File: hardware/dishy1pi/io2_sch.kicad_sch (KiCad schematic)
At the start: 32 parts, among them J6 TerminalBlock_9x2.54mm, J7 TerminalBlock_6x2.54mm, Q3 LTV-847S, Q4 LTV-847S, U10 LTV-847S, U11 LTV-827S-TA1, U12 LTV-817S-TA1

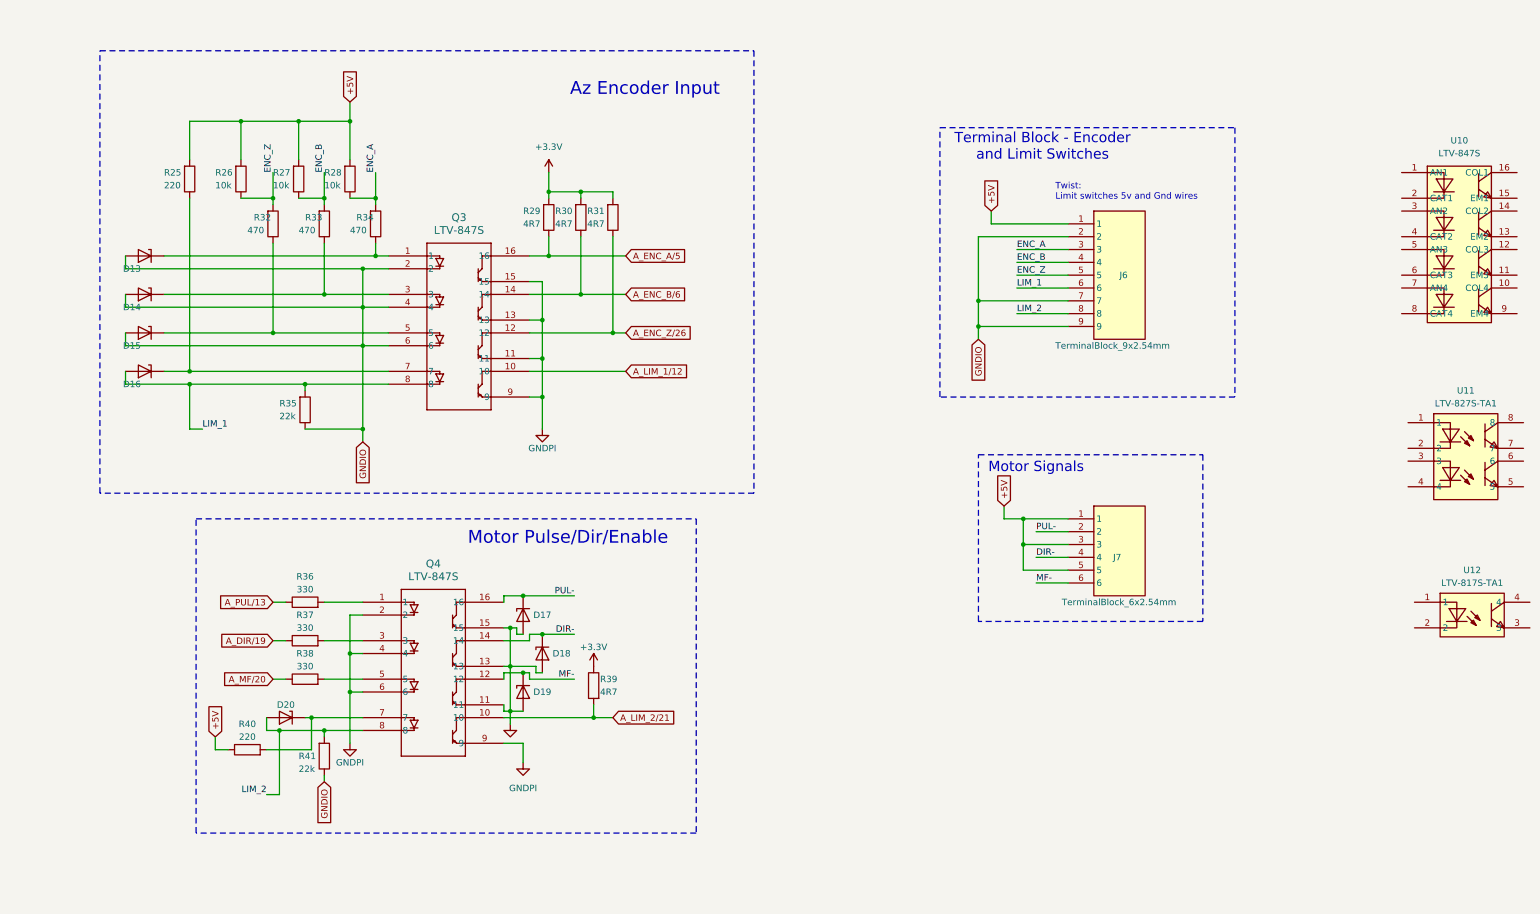
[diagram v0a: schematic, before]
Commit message: Parts place in PCB layout
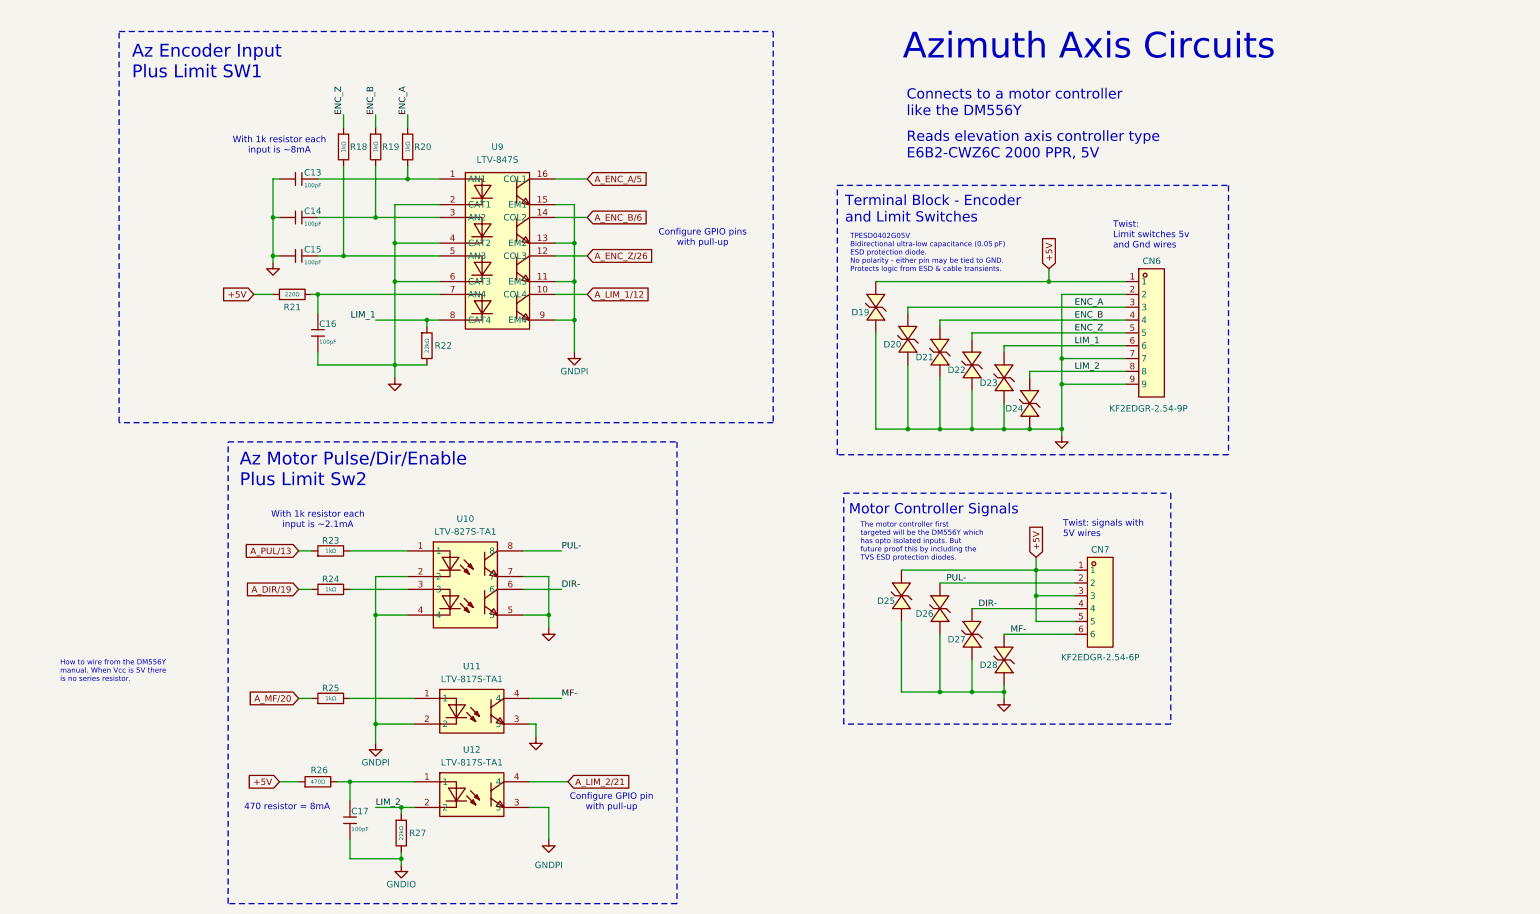
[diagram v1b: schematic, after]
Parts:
- removed D13, D14, D15, D16, D17, D18, D19, D20: TPESD0402G05V, Diode_SMD:D_0402_1005Metric, symbol Diode:PESD5V0L1UL
- removed J6: TerminalBlock_9x2.54mm, DishFootprints:TerminalBlock_9x2.54mm, symbol DishSympols:TerminalBlock_9x2.54mm
- removed J7: TerminalBlock_6x2.54mm, DishFootprints:TerminalBlock_6x2.54mm, symbol DishSympols:TerminalBlock_6x2.54mm
- removed Q3, Q4: LTV-847S, DishFootprints:ACPL-847-300E, symbol DishSympols:ACPL-847-300E
- removed R25, R40: 220, Resistor_SMD:R_0402_1005Metric, symbol Device:R
- removed R26, R27, R28: 10k, Resistor_SMD:R_0402_1005Metric, symbol Device:R
- removed R29, R30, R31, R39: 4R7, Resistor_SMD:R_0402_1005Metric, symbol Device:R
- removed R32, R33, R34: 470, Resistor_SMD:R_0402_1005Metric, symbol Device:R
- removed R35: 22k, Resistor_SMD:R_0201_0603Metric, symbol Device:R
- removed R36, R37, R38: 330, Resistor_SMD:R_0402_1005Metric, symbol Device:R
- removed R41: 22k, Resistor_SMD:R_0402_1005Metric, symbol Device:R
- removed U10: LTV-847S, MyParts:SMD-16_L20.0-W6.5-P2.54-LS10.2-BL, symbol MyParts:LTV-847S
- removed U11: LTV-827S-TA1, MyParts:SMD-8_L9.8-W6.6-P2.54-LS10.3-BL, symbol MyParts:LTV-827S-TA1
- added C13, C14, C15, C16, C17: 100pF, PCM_JLCPCB:C_0402, symbol PCM_JLCPCB-Capacitors:0402,100pF
- added CN6: KF2EDGR-2.54-9P, MyParts:CONN-TH_9P-P2.54_KF2EDGR-2.54-9P, symbol MyParts:KF2EDGR-2.54-9P
- added CN7: KF2EDGR-2.54-6P, MyParts:CONN-TH_KF2EDGR-2.54-6P, symbol MyParts:KF2EDGR-2.54-6P
- added D19, D20, D21, D22, D23, D24, D25, D26, D27, D28: TPESD0402G05V, MyParts:D0402-BI, symbol MyParts:TPESD0402G05V
- added R18, R19, R20, R23, R24, R25: 1kΩ, PCM_JLCPCB:R_0402, symbol PCM_JLCPCB-Resistors:0402,1kΩ
- added R21: 220Ω, PCM_JLCPCB:R_0402, symbol PCM_JLCPCB-Resistors:0402,220Ω
- added R22, R27: 22kΩ, PCM_JLCPCB:R_0402, symbol PCM_JLCPCB-Resistors:0402,22kΩ
- added R26: 470Ω, PCM_JLCPCB:R_0402, symbol PCM_JLCPCB-Resistors:0402,470Ω
- added U10: LTV-827S-TA1, MyParts:LTV827S-TA1, symbol MyParts:LTV-827S-TA1
- added U11: LTV-817S-TA1, MyParts:LTV817S, symbol MyParts:LTV-817S-TA1
- added U9: LTV-847S, myparts:SMD-16_L20.0-W6.5-P2.54-LS10.2-BL, symbol MyParts:LTV-847S
- U12: footprint MyParts:OPTO-SMD-4_L4.6-W6.5-P2.54-LS10.3-BL -> MyParts:LTV817S
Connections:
- net +5V: now also CN6.1, CN7.1, CN7.3, CN7.5, D19.1 (K), D25.1 (K), R21.1, R26.1
- net A_DIR/19: now also R24.1
- net A_ENC_A/5: now also U9.16 (COL1)
- net A_ENC_B/6: now also U9.14 (COL2)
- net A_ENC_Z/26: now also U9.12 (COL3)
- net A_LIM_1/12: now also U9.10 (COL4)
- net A_LIM_2/21: now also U12.4
- net A_MF/20: now also R25.1
- net A_PUL/13: now also R23.1
- net DIR-: now also CN7.4, D27.1 (K), U10.6
- net ENC_A: now also CN6.3, D20.1 (K), R20.1
- net ENC_B: now also CN6.4, D21.1 (K), R19.1
- net ENC_Z: now also CN6.5, D22.1 (K), R18.1
- net GNDIO: now also C13.1, C14.1, C15.1, C16.2, C17.2, CN6.2, CN6.7, CN6.9, D19.2 (A), D20.2 (A), D21.2 (A), D22.2 (A), D23.2 (A), D24.2 (A), D25.2 (A), D26.2 (A), D27.2 (A), D28.2 (A), R22.2, R27.2, U10.5, U10.7, U11.3, U9.2 (CAT1), U9.4 (CAT2), U9.6 (CAT3)
- net GNDPI: now also U12.3, U10.2, U10.4, U11.2, U9.11 (EM3), U9.13 (EM2), U9.15 (EM1), U9.9 (EM4)
- net LIM_1: now also CN6.6, D23.1 (K), R22.1, U9.8 (CAT4)
- net LIM_2: now also U12.2, CN6.8, D24.1 (K), R27.1
- net MF-: now also CN7.6, D28.1 (K), U11.4
- net PUL-: now also CN7.2, D26.1 (K), U10.8
- net at U12.1: now also C17.1, R26.2
- new net: C13.2, R20.2, U9.1 (AN1)
- new net: R23.2, U10.1
- new net: R24.2, U10.3
- new net: C16.1, R21.2, U9.7 (AN4)
- new net: R25.2, U11.1
- new net: C14.2, R19.2, U9.3 (AN2)
- new net: C15.2, R18.2, U9.5 (AN3)
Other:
- note added: "470 resistor = 8mA"
- note added: "Az Encoder Input Plus Limit SW1"
- note added: "Az Motor Pulse/Dir/Enable Plus Limit Sw2"
- note added: "Azimuth Axis Circuits"
- note added: "Configure GPIO pin with pull-up"
- note added: "Configure GPIO pins with pull-up"
- note added: "Connects to a motor controller like the DM556Y"
- note added: "How to wire from the DM556Y manual. When Vcc is 5V there is no series resistor."
- note added: "Motor Controller Signals"
- note added: "Reads elevation axis controller type E6B2-CWZ6C 2000 PPR, 5V"
- note added: "TPESD0402G05V Bidirectional ultra-low capacitance (0.05 pF) ESD protection diode. No polarity - either pin may be tied to GND. Protects logic from ESD & cable transients."
- note added: "The motor controller first targeted will be the DM556Y which has opto isolated inputs. But future proof this by including the TVS ESD protection diodes."
- note added: "Twist: signals with 5V wires"
- note added: "With 1k resistor each input is ~2.1mA"
- note added: "With 1k resistor each input is ~8mA"
- note removed: "Az Encoder Input"
- note removed: "Motor Pulse/Dir/Enable"
- note removed: "Motor Signals"
- company: (none) -> JRDish

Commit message: Ground and Power planes placed
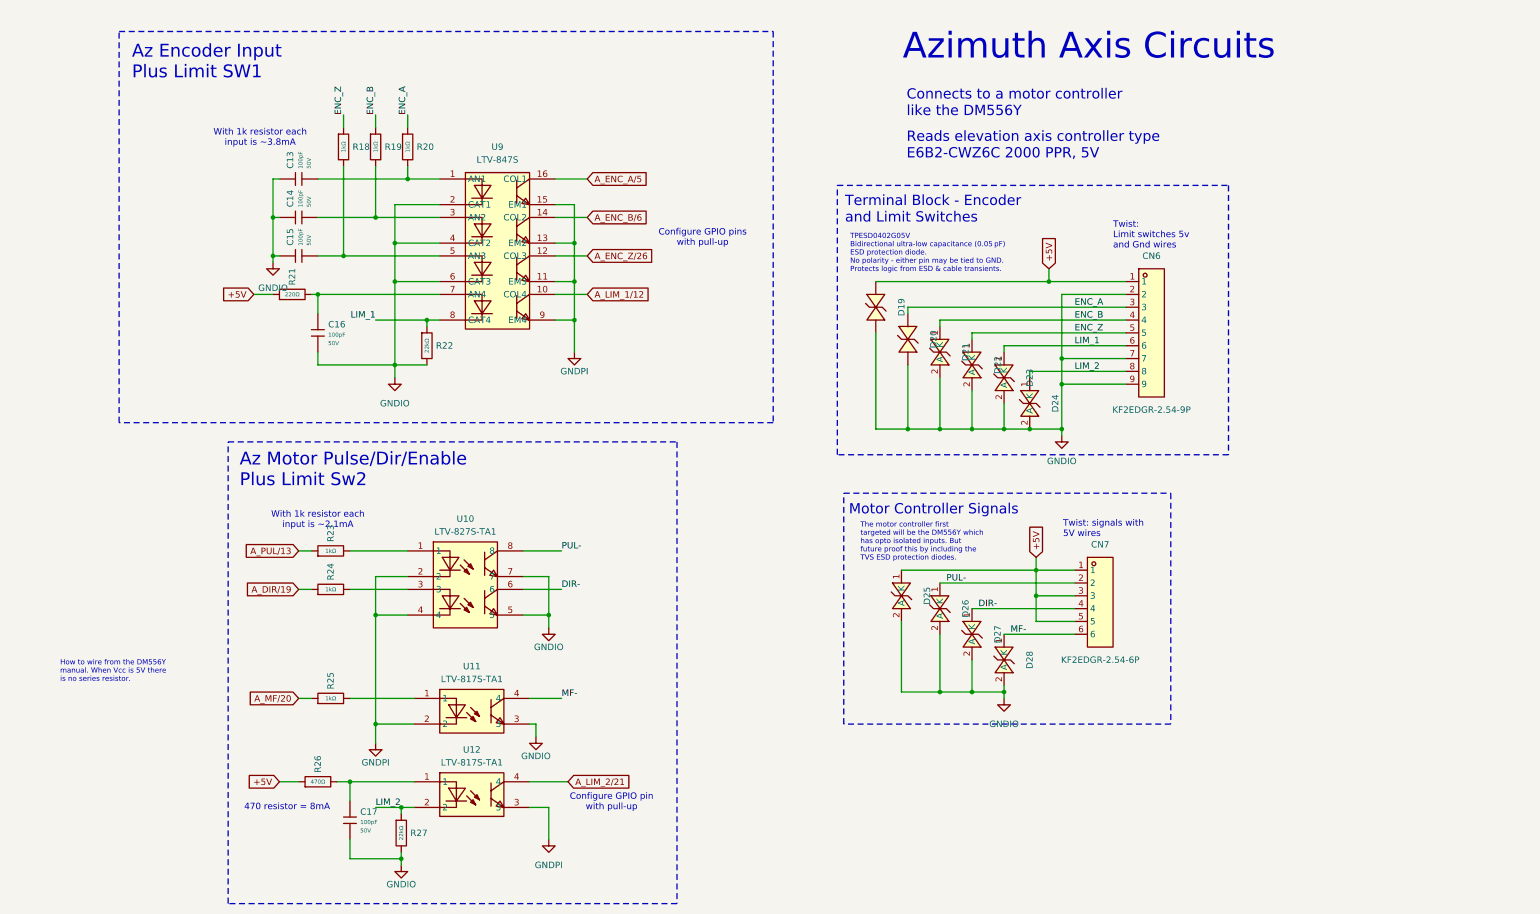
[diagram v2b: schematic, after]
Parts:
- U9: footprint myparts:SMD-16_L20.0-W6.5-P2.54-LS10.2-BL -> MyParts:SMD-16_L20.0-W6.5-P2.54-LS10.2-BL
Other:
- note added: "With 1k resistor each input is ~3.8mA"
- note removed: "With 1k resistor each input is ~8mA"
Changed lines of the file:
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@@
 		)
 	)
-	(text "With 1k resistor each \ninput is ~8mA"
+	(text "With 1k resistor each \ninput is ~3.8mA"
 		(exclude_from_sim no)
-		(at 68.58 44.196 0)
+		(at 64.77 42.672 0)
 		(effects
 			(font
@@
 		(dnp no)
 		(property "Reference" "D21"
-			(at 196.342 86.106 90)
+			(at 204.47 85.09 0)
 			(effects
 				(font
@@
 		(dnp no)
 		(property "Reference" "D27"
-			(at 202.692 141.986 90)
+			(at 210.82 140.97 0)
 			(effects
 				(font
@@
 		(dnp no)
 		(property "Reference" "R26"
-			(at 76.454 167.894 90)
+			(at 76.2 168.402 0)
 			(effects
 				(font
 					(size 1.27 1.27)
 				)
+				(justify left)
 			)
 		)
@@
 		(dnp no)
 		(property "Reference" "D25"
-			(at 188.722 134.366 90)
+			(at 196.85 133.35 0)
 			(effects
 				(font
@@
 	)
 	(symbol
+		(lib_name "TPESD0402G05V_2")
 		(lib_id "MyParts:TPESD0402G05V")
 		(at 186.69 76.2 270)
@@
 		(dnp no)
 		(property "Reference" "D19"
-			(at 183.642 77.216 90)
+			(at 191.77 76.2 0)
 			(effects
 				(font
@@
 		(dnp no)
 		(property "Reference" "D22"
-			(at 202.692 88.646 90)
+			(at 210.82 87.63 0)
 			(effects
 				(font
@@
 					(size 1.27 1.27)
 				)
-				(hide yes)
 			)
 		)
@@
 		(dnp no)
 		(fields_autoplaced yes)
-		(property "Reference" "#PWR039"
+		(property "Reference" "#PWR39"
 			(at 212.09 160.02 0)
 			(effects
@@
 		)
 		(property "Value" "GNDIO"
-			(at 212.0899 157.48 90)
+			(at 212.09 158.75 0)
 			(effects
 				(font
 					(size 1.27 1.27)
 				)
-				(justify right)
-				(hide yes)
 			)
 		)
@@
 			(project "DishyPi1"
 				(path "/e63e39d7-6ac0-4ffd-8aa3-1841a4541b55/ce2ab250-a57c-49c3-a7e8-2e9dc039f394"
-					(reference "#PWR039")
+					(reference "#PWR39")
 					(unit 1)
 				)
@@
 		(dnp no)
 		(property "Reference" "R20"
-			(at 95.25 44.45 0)
+			(at 95.758 44.45 0)
 			(effects
 				(font
@@
 					(size 1.27 1.27)
 				)
-				(hide yes)
 			)
 		)
@@
 		(dnp no)
 		(property "Reference" "R22"
-			(at 99.314 83.82 0)
+			(at 99.568 83.82 0)
 			(effects
 				(font
@@
 	)
 	(symbol
+		(lib_name "TPESD0402G05V_1")
 		(lib_id "MyParts:TPESD0402G05V")
 		(at 193.04 82.55 270)
@@
 		(dnp no)
 		(property "Reference" "D20"
-			(at 189.992 83.566 90)
+			(at 198.12 82.55 0)
 			(effects
 				(font
@@
 		(dnp no)
 		(property "Reference" "CN7"
-			(at 231.14 124.206 0)
+			(at 231.14 123.19 0)
 			(effects
 				(font
@@
 		)
 		(property "Value" "KF2EDGR-2.54-6P"
-			(at 231.14 145.542 0)
+			(at 231.14 146.05 0)
 			(effects
 				(font
@@
 		(dnp no)
 		(fields_autoplaced yes)
-		(property "Reference" "#PWR038"
+		(property "Reference" "#PWR38"
 			(at 223.52 107.95 0)
 			(effects
@@
 		)
 		(property "Value" "GNDIO"
-			(at 223.5199 105.41 90)
+			(at 223.52 106.68 0)
 			(effects
 				(font
 					(size 1.27 1.27)
 				)
-				(justify right)
-				(hide yes)
 			)
 		)
@@
 			(project "DishyPi1"
 				(path "/e63e39d7-6ac0-4ffd-8aa3-1841a4541b55/ce2ab250-a57c-49c3-a7e8-2e9dc039f394"
-					(reference "#PWR038")
+					(reference "#PWR38")
 					(unit 1)
 				)
@@
 		(dnp no)
 		(property "Reference" "R21"
-			(at 71.12 76.2 90)
+			(at 71.12 71.882 0)
 			(effects
 				(font
 					(size 1.27 1.27)
 				)
+				(justify left)
 			)
 		)
@@
 		(dnp no)
 		(property "Reference" "R24"
-			(at 78.74 130.048 90)
+			(at 78.74 130.302 0)
 			(effects
 				(font
 					(size 1.27 1.27)
 				)
+				(justify left)
 			)
 		)
@@
 		(dnp no)
 		(property "Reference" "R23"
-			(at 78.74 122.428 90)
+			(at 78.74 122.682 0)
 			(effects
 				(font
 					(size 1.27 1.27)
 				)
+				(justify left)
 			)
 		)
@@
 		(dnp no)
 		(property "Reference" "R27"
-			(at 94.234 180.34 0)
+			(at 94.488 180.34 0)
 			(effects
 				(font
@@
 		(dnp no)
 		(property "Reference" "D24"
-			(at 214.122 96.266 90)
+			(at 222.25 95.25 0)
 			(effects
 				(font
@@
 		(dnp no)
 		(property "Reference" "C14"
-			(at 75.184 57.15 90)
+			(at 70.722 56.388 0)
 			(effects
 				(font
 					(size 1.27 1.27)
 				)
+				(justify left)
 			)
 		)
 		(property "Value" "100pF"
-			(at 75.184 59.69 90)
+			(at 72.7682 56.388 0)
 			(effects
 				(font
 					(size 0.8 0.8)
 				)
+				(justify left)
 			)
 		)
@@
 		)
 		(property "Voltage Rated" "50V"
-			(at 74.93 55.88 0)
+			(at 74.4362 56.388 0)
 			(effects
 				(font
@@
 				)
 				(justify left)
-				(hide yes)
 			)
 		)
@@
 		(dnp no)
 		(property "Reference" "C15"
-			(at 75.184 64.77 90)
+			(at 70.722 64.008 0)
 			(effects
 				(font
 					(size 1.27 1.27)
 				)
+				(justify left)
 			)
 		)
 		(property "Value" "100pF"
-			(at 75.184 67.31 90)
+			(at 72.7682 64.008 0)
 			(effects
 				(font
 					(size 0.8 0.8)
 				)
+				(justify left)
 			)
 		)
@@
 		)
 		(property "Voltage Rated" "50V"
-			(at 74.93 63.5 0)
+			(at 74.4362 64.008 0)
 			(effects
 				(font
@@
 				)
 				(justify left)
-				(hide yes)
 			)
 		)
@@
 		(dnp no)
 		(property "Reference" "C13"
-			(at 75.184 49.53 90)
+			(at 70.722 48.768 0)
 			(effects
 				(font
 					(size 1.27 1.27)
 				)
+				(justify left)
 			)
 		)
 		(property "Value" "100pF"
-			(at 75.184 52.07 90)
+			(at 72.7682 48.768 0)
 			(effects
 				(font
 					(size 0.8 0.8)
 				)
+				(justify left)
 			)
 		)
@@
 		)
 		(property "Voltage Rated" "50V"
-			(at 74.93 48.26 0)
+			(at 74.4362 48.768 0)
 			(effects
 				(font
@@
 				)
 				(justify left)
-				(hide yes)
 			)
 		)
@@
 		(dnp no)
 		(property "Reference" "CN6"
-			(at 239.522 67.056 0)
+			(at 241.3 66.04 0)
 			(effects
 				(font
 					(size 1.27 1.27)
 				)
-				(justify left)
 			)
 		)
 		(property "Value" "KF2EDGR-2.54-9P"
-			(at 232.918 96.266 0)
+			(at 241.3 96.52 0)
 			(effects
 				(font
 					(size 1.27 1.27)
 				)
-				(justify left)
 			)
 		)
@@
 		(dnp no)
 		(property "Reference" "C16"
-			(at 76.454 79.502 0)
+			(at 78.232 79.612 0)
 			(effects
 				(font
@@
 		)
 		(property "Value" "100pF"
-			(at 76.454 83.058 0)
+			(at 78.232 81.6582 0)
 			(effects
 				(font
@@
 		)
 		(property "Voltage Rated" "50V"
-			(at 78.74 83.82 0)
+			(at 78.232 83.3262 0)
 			(effects
 				(font
@@
 				)
 				(justify left)
-				(hide yes)
 			)
 		)
@@
 		(dnp no)
 		(property "Reference" "D28"
-			(at 209.042 147.066 90)
+			(at 217.17 146.05 0)
 			(effects
 				(font
@@
 					(size 1.27 1.27)
 				)
-				(hide yes)
 			)
 		)
@@
 					(size 1.27 1.27)
 				)
-				(hide yes)
 			)
 		)
@@
 		(dnp no)
 		(property "Reference" "R19"
-			(at 88.9 44.45 0)
+			(at 89.408 44.45 0)
 			(effects
 				(font
@@
 			)
 		)
-		(property "Footprint" "myparts:SMD-16_L20.0-W6.5-P2.54-LS10.2-BL"
+		(property "Footprint" "MyParts:SMD-16_L20.0-W6.5-P2.54-LS10.2-BL"
 			(at 111.76 86.36 0)
 			(effects
@@
 		(dnp no)
 		(property "Reference" "C17"
-			(at 82.804 176.022 0)
+			(at 84.582 176.132 0)
 			(effects
 				(font
@@
 		)
 		(property "Value" "100pF"
-			(at 82.804 179.578 0)
+			(at 84.582 178.1782 0)
 			(effects
 				(font
@@
 		)
 		(property "Voltage Rated" "50V"
-			(at 85.09 180.34 0)
+			(at 84.582 179.8462 0)
 			(effects
 				(font
@@
 				)
 				(justify left)
-				(hide yes)
 			)
 		)
@@
 		(dnp no)
 		(property "Reference" "D23"
-			(at 209.042 91.186 90)
+			(at 217.17 90.17 0)
 			(effects
 				(font
@@
 		(dnp no)
 		(property "Reference" "R18"
-			(at 82.55 44.45 0)
+			(at 83.058 44.45 0)
 			(effects
 				(font
@@
 		(dnp no)
 		(property "Reference" "R25"
-			(at 78.74 151.638 90)
+			(at 78.74 151.892 0)
 			(effects
 				(font
 					(size 1.27 1.27)
 				)
+				(justify left)
 			)
 		)
@@
 		(dnp no)
 		(property "Reference" "D26"
-			(at 196.342 136.906 90)
+			(at 204.47 135.89 0)
 			(effects
 				(font
